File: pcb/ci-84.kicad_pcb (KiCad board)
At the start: 2 copper layers, 103.8 x 199.5 mm, 113 parts, among them J1 Conn_01x02, SW1 SW_Push, SW10 XT0N, SW11 STAT, SW12 MATH, SW13 APPS, SW14 PRGM, SW15 VARS, SW16 CLEAR, SW17 X^-1, SW18 SIN, SW19 COS, SW2 Y=, SW20 TAN, SW21 ^, SW22 X^2, SW23 ,, SW24 (, SW25 ), SW26 DIVIDE, SW27 LOG, SW28 7, SW29 8, SW3 WINDOW, SW30 9, SW31 MULITPLY, SW32 IN, SW33 4, SW34 5, SW35 6, SW36 SUBTRACT, SW37 STO, SW38 1, SW39 2, SW4 ZOOM, SW40 3, SW41 ADD, SW42 ON, SW43 0, SW44 ., SW45 (-), SW46 ENTER, SW47 GRAPH, SW48 UP, SW49 RIGHT, SW5 TRACE, SW50 DOWN, SW51 LEFT, SW6 2ND, SW7 MODE, SW8 DEL, SW9 ALPHA, U1 STM32L471RGTx, U3 TPS63900, U4 TFT_320x240

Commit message: finish some stuff idk
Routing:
- removed copper zone on B.Cu, net GND
- removed copper zone on F.Cu, net GND
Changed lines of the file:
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@@
 		(tags "capacitor")
 		(property "Reference" "C11"
-			(at 0.245 -1.94 360)
+			(at 0.245 -1.94 0)
 			(layer "B.SilkS")
 			(effects
@@
 		)
 		(property "Value" "10u"
-			(at 0 -1.68 360)
+			(at 0 -1.68 0)
 			(layer "B.Fab")
 			(effects
@@
 		)
 		(fp_text user "${REFERENCE}"
-			(at 0 0 360)
+			(at 0 0 0)
 			(layer "B.Fab")
 			(effects
@@
 		(net 132)
 	)
-	(zone
-		(net 2)
-		(net_name "GND")
-		(layers "F&B.Cu")
-		(hatch edge 0.5)
-		(connect_pads
-			(clearance 0.2)
-		)
-		(min_thickness 0.25)
-		(filled_areas_thickness no)
-		(fill
-			(thermal_gap 0.5)
-			(thermal_bridge_width 0.5)
-		)
-		(polygon
-			(pts
-				(xy 220.85 81.225) (xy 339.4 83.95) (xy 343.775 292.75) (xy 218.675 291.65)
-			)
-		)
-	)
 )

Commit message: more keyboarD
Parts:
- moved SW42 93.8 mm to (169.4, 253.3)
- moved D32 93.8 mm to (163.3, 240.3)
- moved D37 93.8 mm to (163.4, 248.2)
- moved D27 93.8 mm to (163.2, 232.5)
- moved D42 93.8 mm to (163.2, 254.9)
- moved SW27 93.8 mm to (169.3, 230.9)
- moved SW32 93.8 mm to (169.3, 238.8)
- moved SW37 93.8 mm to (169.3, 246.6)
- moved D30 87.6 mm to (205.9, 232.6)
- moved D35 87.6 mm to (205.9, 240.4)
- moved SW28 87.6 mm to (187.5, 231.0)
- moved SW29 87.6 mm to (199.9, 231.0)
- moved SW30 87.6 mm to (211.9, 231.0)
- moved SW33 87.6 mm to (187.5, 238.8)
- moved SW34 87.6 mm to (199.9, 238.8)
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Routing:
- net Net-(SW12-Pad2): track 62.3 -> 177.8 mm, vias 16 -> 8
- net Net-(D22-K): track 48.4 -> 85.4 mm
- net Net-(SW15-Pad2): track 88.2 -> 52.1 mm
- net Net-(D17-K): track 48.3 -> 84.3 mm
- net Net-(SW16-Pad2): track 68.7 -> 37.8 mm
- net Net-(SW11-Pad2): track 62.7 -> 33.1 mm, vias 12 -> 10
- net Net-(SW10-Pad2): track 62.6 -> 35.8 mm, vias 16 -> 11
- net Net-(D12-K): track 48.5 -> 72.2 mm
- net Net-(D10-K): track 24.0 -> 35.8 mm
- net Net-(D1-K): track 48.1 -> 54.2 mm
- net Net-(D11-A): track 2.40 -> 0.00 mm
- net Net-(D14-A): track 2.26 -> 0.00 mm
- net Net-(D19-A): track 2.25 -> 0.00 mm
- net Net-(D17-A): track 2.17 -> 0.00 mm
- net Net-(D21-A): track 2.13 -> 0.00 mm
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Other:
- board size 103.8 x 199.5 mm -> 91 x 206.8 mm

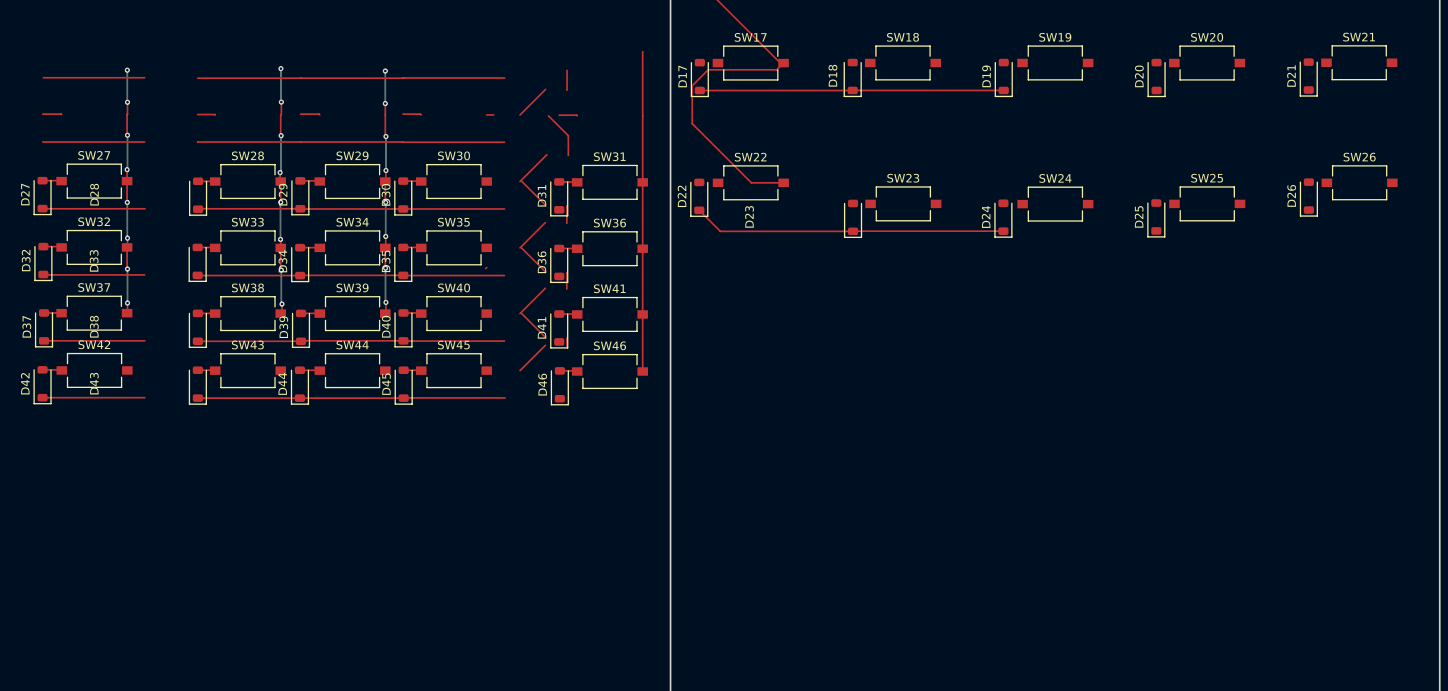
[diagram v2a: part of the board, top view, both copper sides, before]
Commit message: add missing outline rows
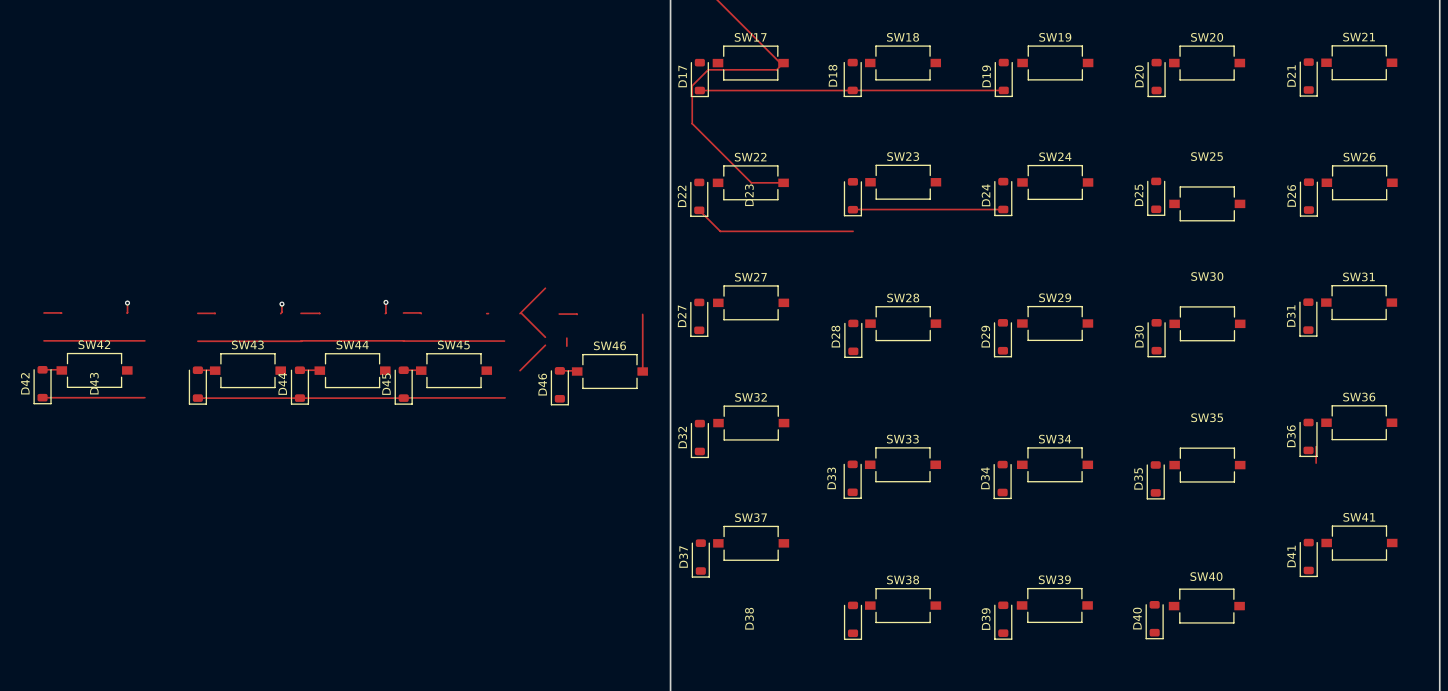
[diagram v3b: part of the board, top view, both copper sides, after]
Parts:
- moved SW40 95.5 mm to (300.9, 281.2)
- moved D40 95.3 mm to (294.8, 282.7)
- moved SW35 92.8 mm to (301.0, 264.5)
- moved D41 92.7 mm to (313.0, 275.4)
- moved SW41 92.7 mm to (319.0, 273.8)
- moved D35 92.7 mm to (294.9, 266.2)
- moved D36 91.0 mm to (313.0, 261.1)
- moved SW36 91.0 mm to (319.0, 259.5)
- moved SW30 90.7 mm to (301.0, 247.8)
- moved D30 90.7 mm to (295.0, 249.3)
- moved D39 90.0 mm to (276.9, 282.8)
- moved SW39 90.0 mm to (283.0, 281.1)
- moved D31 89.8 mm to (313.0, 246.9)
- moved SW31 89.8 mm to (319.0, 245.3)
- moved D34 87.0 mm to (276.8, 266.1)
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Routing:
- net Net-(D27-K): track 48.4 -> 0.00 mm
- net Net-(D22-K): track 85.4 -> 37.0 mm
- net Net-(D32-K): track 48.3 -> 0.00 mm
- net Net-(D17-K): track 84.3 -> 36.0 mm
- net Net-(SW15-Pad2): track 52.1 -> 19.7 mm
- net Net-(SW16-Pad2): track 37.8 -> 6.75 mm
- net Net-(SW10-Pad2): track 35.8 -> 7.78 mm, vias 11 -> 4
- net Net-(SW12-Pad2): track 177.8 -> 150.0 mm, vias 8 -> 1
- net Net-(SW11-Pad2): track 33.1 -> 5.63 mm, vias 10 -> 3
- net Net-(D34-A): track 2.34 -> 0.00 mm
- net Net-(D29-A): track 2.33 -> 0.00 mm
- net Net-(D24-A): track 2.32 -> 0.00 mm
- net Net-(D27-A): track 2.27 -> 0.00 mm
- net Net-(D22-A): track 2.25 -> 0.00 mm
- net Net-(D25-A): track 2.19 -> 0.00 mm
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
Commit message: finish keyboard matrix
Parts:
- moved D45 99.7 mm to (295.1, 299.5)
- moved SW45 99.7 mm to (301.0, 297.9)
- moved D46 95.2 mm to (313.1, 289.5)
- moved SW46 95.2 mm to (319.0, 287.9)
- moved SW44 94.3 mm to (283.0, 297.9)
- moved D44 94.3 mm to (276.8, 299.5)
- moved SW43 89.4 mm to (265.0, 297.9)
- moved D43 89.4 mm to (259.1, 299.5)
- moved SW42 85.0 mm to (247.0, 287.9)
- moved D42 85.0 mm to (240.8, 289.5)
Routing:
- net Net-(SW12-Pad2): track 150.0 -> 262.4 mm, vias 1 -> 0
- net Net-(D37-K): track 48.2 -> 21.1 mm
- net Net-(D42-K): track 48.5 -> 22.4 mm
- net Net-(D32-K): track 0.00 -> 20.1 mm
- net Net-(D27-K): track 0.00 -> 19.3 mm
- net Net-(SW15-Pad2): track 19.7 -> 6.06 mm
- net Net-(SW16-Pad2): track 6.75 -> 0.00 mm
- net Net-(D44-A): track 2.37 -> 0.00 mm
- net Net-(D42-A): track 2.31 -> 0.00 mm
- net Net-(D39-A): track 2.24 -> 0.00 mm
- net Net-(D41-A): track 2.15 -> 0.00 mm
- net Net-(D40-A): track 2.13 -> 0.00 mm
- net Net-(D45-A): track 2.10 -> 0.00 mm
- net Net-(D37-A): track 2.09 -> 0.00 mm
- net Net-(D46-A): track 2.08 -> 0.00 mm
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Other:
- board size 91 x 206.8 mm -> 91 x 217 mm

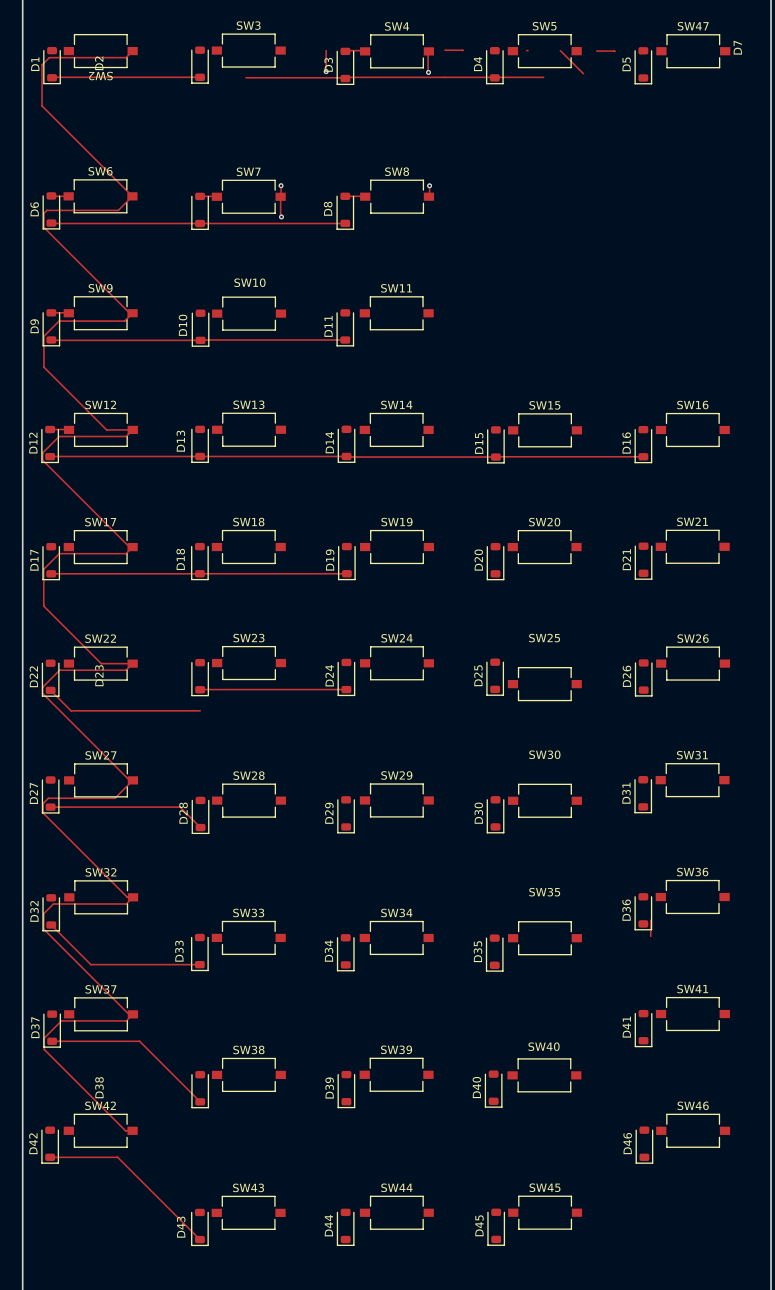
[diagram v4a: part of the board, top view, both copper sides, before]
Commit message: finish wiring matrix
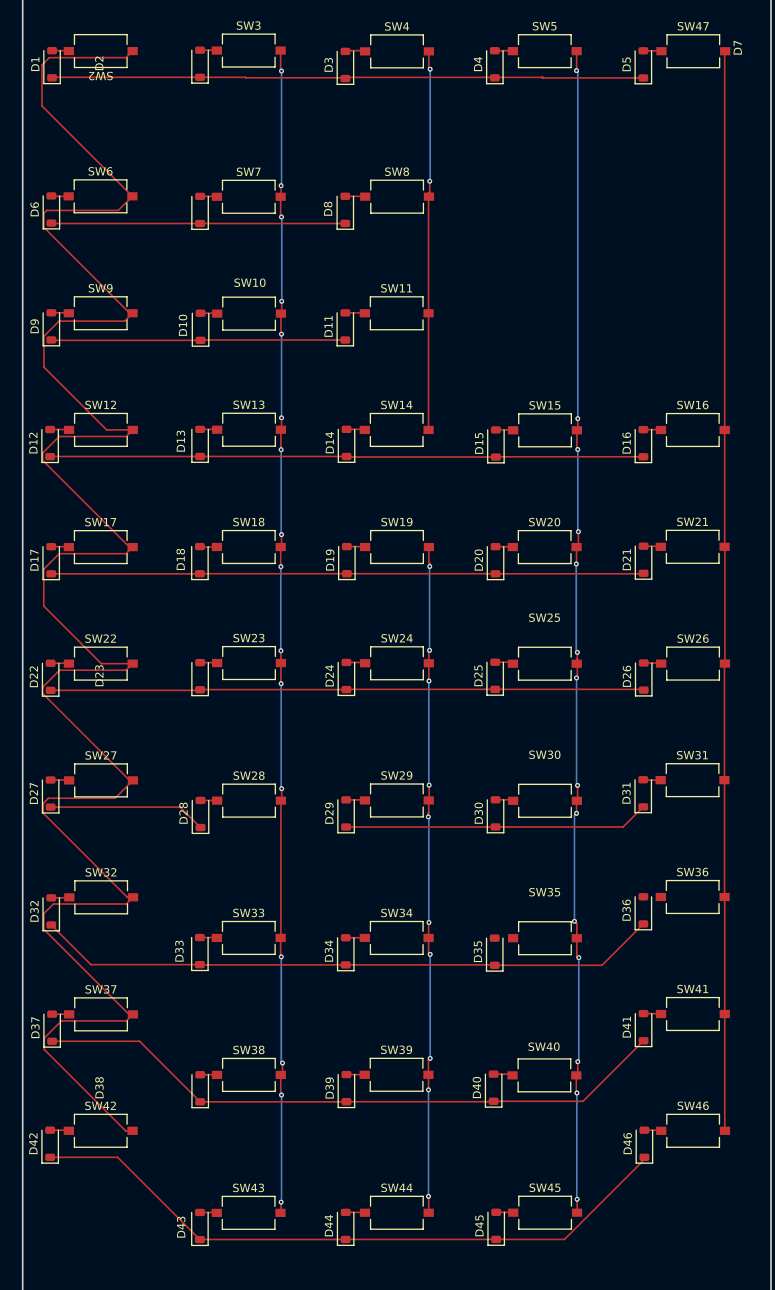
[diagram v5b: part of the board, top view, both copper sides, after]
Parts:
- moved SW25 2.48 mm to (301.0, 231.2)
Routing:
- net Net-(SW15-Pad2): track 6.06 -> 142.9 mm, vias 0 -> 14
- net Net-(SW10-Pad2): track 6.48 -> 142.1 mm, vias 3 -> 16
- net Net-(SW16-Pad2): track 0.00 -> 131.4 mm
- net Net-(SW11-Pad2): track 4.20 -> 128.3 mm, vias 2 -> 12
- net Net-(D42-K): track 22.4 -> 80.7 mm
- net Net-(D37-K): track 21.1 -> 78.0 mm
- net Net-(D32-K): track 20.1 -> 76.1 mm
- net Net-(D27-K): track 19.3 -> 56.4 mm
- net Net-(D17-K): track 36.0 -> 72.1 mm
- net Net-(D22-K): track 37.0 -> 72.2 mm
- net Net-(D1-K): track 54.2 -> 72.2 mm
- net Net-(D11-A): track 0.00 -> 2.40 mm
- net Net-(D44-A): track 0.00 -> 2.37 mm
- net Net-(D40-A): track 0.00 -> 2.36 mm
- net Net-(D34-A): track 0.00 -> 2.34 mm
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
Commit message: update outline, add arrow keys
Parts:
- moved SW51 44.4 mm to (300.7, 172.7)
- moved SW49 42.1 mm to (319.3, 172.7)
- moved SW50 42.0 mm to (310.0, 178.7)
- moved SW48 42.0 mm to (310.0, 166.7)
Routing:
- net Net-(SW16-Pad2): track 131.4 -> 131.6 mm, vias 0 -> 2

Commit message: add correct spaing
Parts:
- moved SW48 8.42 mm to (310.0, 175.1)
- moved SW49 8.42 mm to (319.3, 181.1)
- moved SW50 8.42 mm to (310.0, 187.1)
- moved SW51 8.42 mm to (300.7, 181.1)

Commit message: fix missing connections
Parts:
- moved SW1 39.0 mm to (314.8, 146.7), turned to 0 degrees
- moved J1 31.2 mm to (255.4, 147.9)
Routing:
- net /IO_DC: track 0.81 -> 61.9 mm
- net +BATT: track 8.78 -> 67.8 mm, vias 0 -> 1
- net VDD: track 45.2 -> 99.4 mm
- net /TS_MISO: track 0.00 -> 53.8 mm
- net /SPI_CS: track 0.00 -> 53.0 mm, vias 0 -> 2
- net /TS_CS: track 0.00 -> 51.1 mm
- net /TS_CK: track 0.00 -> 48.1 mm, vias 0 -> 1
- net /TS_MOSI: track 0.00 -> 47.3 mm
- net /SPI3_MOSI: track 0.00 -> 46.6 mm
- net /SPI3_SCK: track 0.00 -> 46.6 mm
- net /SPI_MISO: track 0.00 -> 45.7 mm, vias 0 -> 1
- net /SCREEN_RST: track 0.00 -> 42.3 mm, vias 0 -> 1
- net /IO_LED: track 0.00 -> 37.6 mm, vias 0 -> 1
- net Net-(U1-NRST): track 17.5 -> 43.4 mm
- net Net-(D27-K): track 56.4 -> 74.1 mm
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- added copper zone on B.Cu, net GND
- added copper zone on F.Cu, net GND
